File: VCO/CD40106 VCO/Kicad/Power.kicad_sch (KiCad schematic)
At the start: 0 parts

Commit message: Schem finished (no 2nd board added yet)
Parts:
- added C? (x2): 10µ, Capacitor_THT:CP_Radial_D5.0mm_P2.00mm, symbol Device:CP1_Small
- added C? (x7): 100nF, Capacitor_THT:C_Disc_D7.0mm_W2.5mm_P5.00mm, symbol Device:C_Small
- added D?: LED-12V, LED_THT:LED_D4.0mm, symbol Device:LED
- added FB? (x2): 10R, Inductor_THT:L_Axial_L9.5mm_D4.0mm_P12.70mm_Horizontal_Fastron_SMCC, symbol Device:Ferrite_Bead_Small
- added J?: Power Input, Connector_IDC:IDC-Header_2x05_P2.54mm_Vertical, symbol Connector:Conn_01x10_Male
- added R?: 2.2k, Resistor_THT:R_Axial_DIN0207_L6.3mm_D2.5mm_P10.16mm_Horizontal, symbol Device:R
- added U? (x6): 40106, symbol 4xxx:40106
- added U? (x2): TL074, Package_DIP:DIP-14_W7.62mm_Socket, symbol Amplifier_Operational:TL074
- added U?: LM13700, Package_SO:SOIC-16_3.9x9.9mm_P1.27mm, symbol Amplifier_Operational:LM13700
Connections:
- new net: D?.2 (A), R?.2
- new net: FB?.2, J?.1 (Pin_1), J?.2 (Pin_2)
- new net: FB?.2, J?.10 (Pin_10), J?.9 (Pin_9)
- new net +12V: C?.1, C?.1, C?.1, C?.1, C?.1, FB?.1, R?.1, U?.11 (V+), U?.14 (VDD), U?.4 (V+), U?.4 (V+)
- new net -12V: C?.2, C?.2, C?.2, C?.2, FB?.1, U?.11 (V-), U?.11 (V-), U?.6 (V-)
- new net GND: C?.1, C?.1, C?.1, C?.1, C?.2, C?.2, C?.2, C?.2, C?.2, D?.1 (K), J?.3 (Pin_3), J?.4 (Pin_4), J?.5 (Pin_5), J?.6 (Pin_6), J?.7 (Pin_7), J?.8 (Pin_8), U?.11, U?.13, U?.3, U?.5, U?.7 (VSS), U?.9

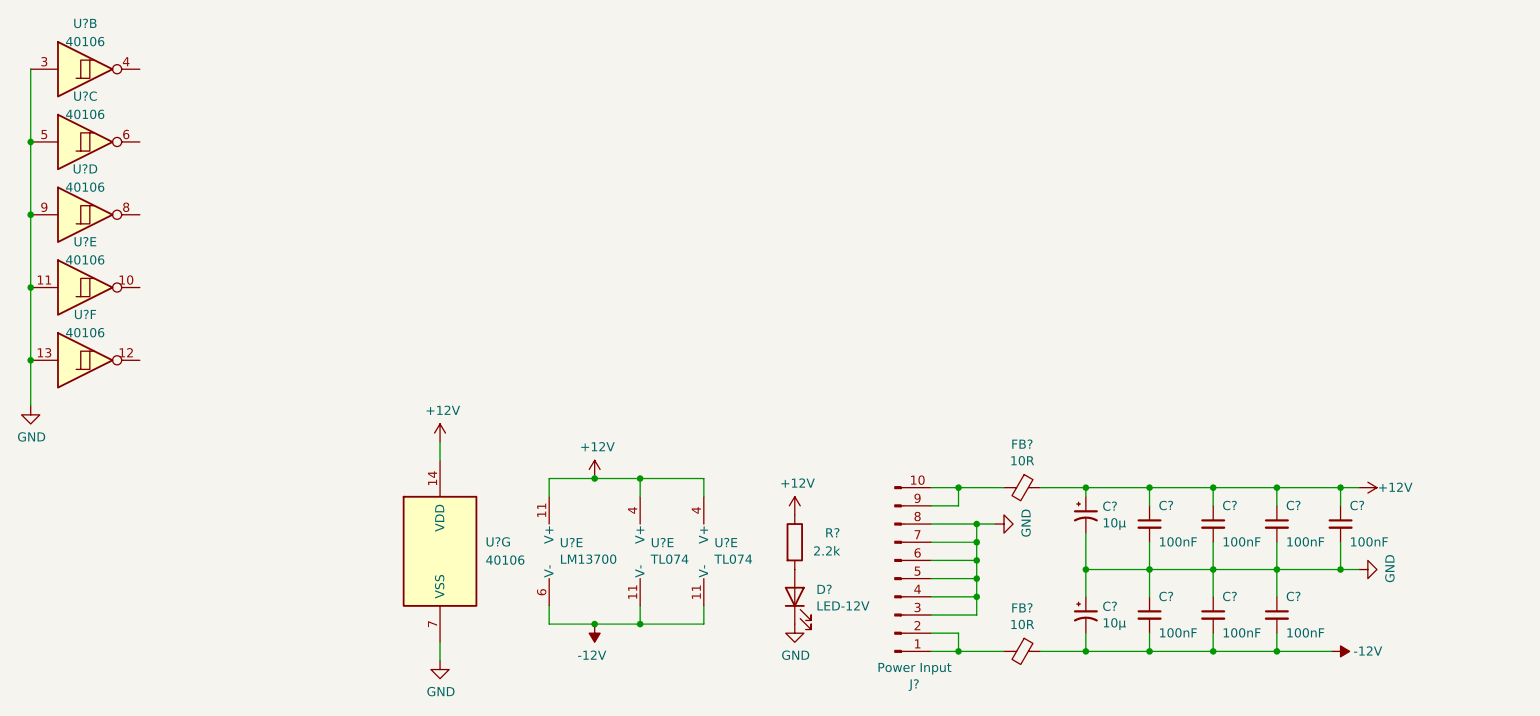
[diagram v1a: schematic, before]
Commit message: added connectors between boards
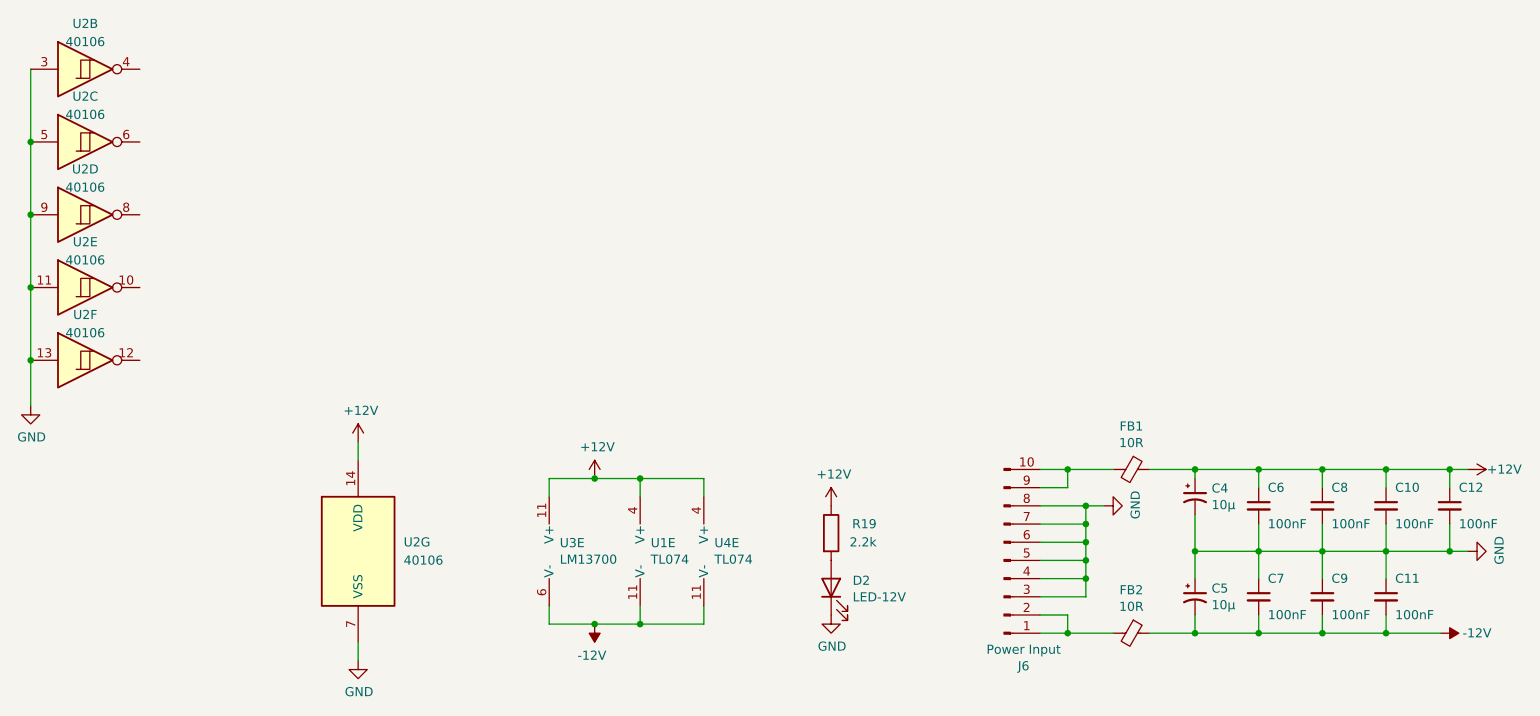
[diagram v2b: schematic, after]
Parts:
- gave numbers to parts that had none: 18
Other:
- moved on the sheet: C10, C11, C12, C4, C5, C6, C7, C8, C9, D2, FB1, FB2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
